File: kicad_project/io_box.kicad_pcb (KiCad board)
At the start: 4 copper layers, 200 x 120 mm, 76 parts, among them J1 24V, J10 24V, J2 GND, J3 Conn_01x02, J4 Output, J5 Digital Input, J6 5V, J7 12V, J8 NC, J9 GND, Q1 2N3904, Q2 2N3904, Q3 2N3904, Q4 2N3904, SW1 SW_Push, SW10 SW_Push, SW2 SW_Push, SW3 SW_Push, SW4 SW_SPDT, SW5 SW_SPDT, SW6 SW_DIP_x04, SW7 SW_SPDT, SW8 SW_DIP_x04, SW9 SW_SPDT, U1 R-78E5.0-1.0, U2 SN74AC14N, U3 R-78E12-1.0/X9

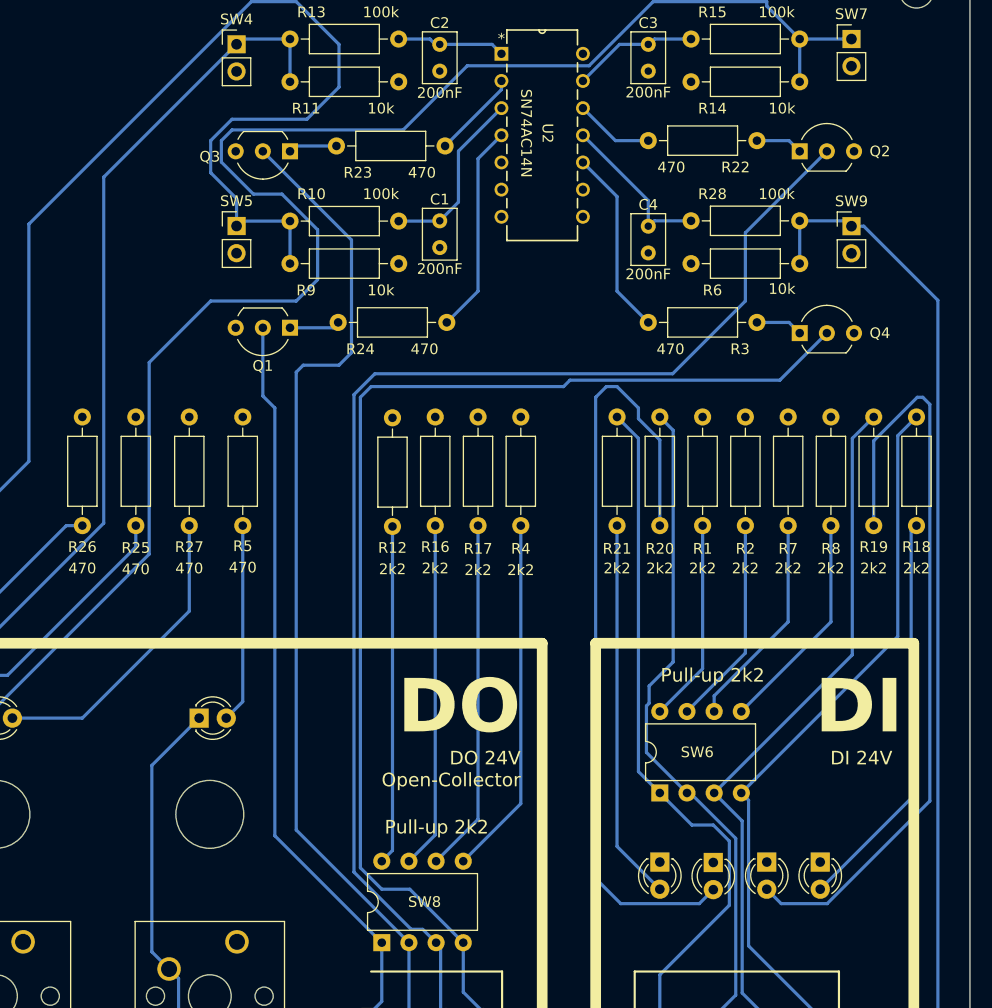
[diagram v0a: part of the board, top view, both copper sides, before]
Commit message: Bug fixes and resistor changes
Raised LED resistor values from 470 to 2k2 and from 2k2 to 10k.
Fixed NPN transistor incorrect pin order.
Fixed LPTA connector footprint pins.
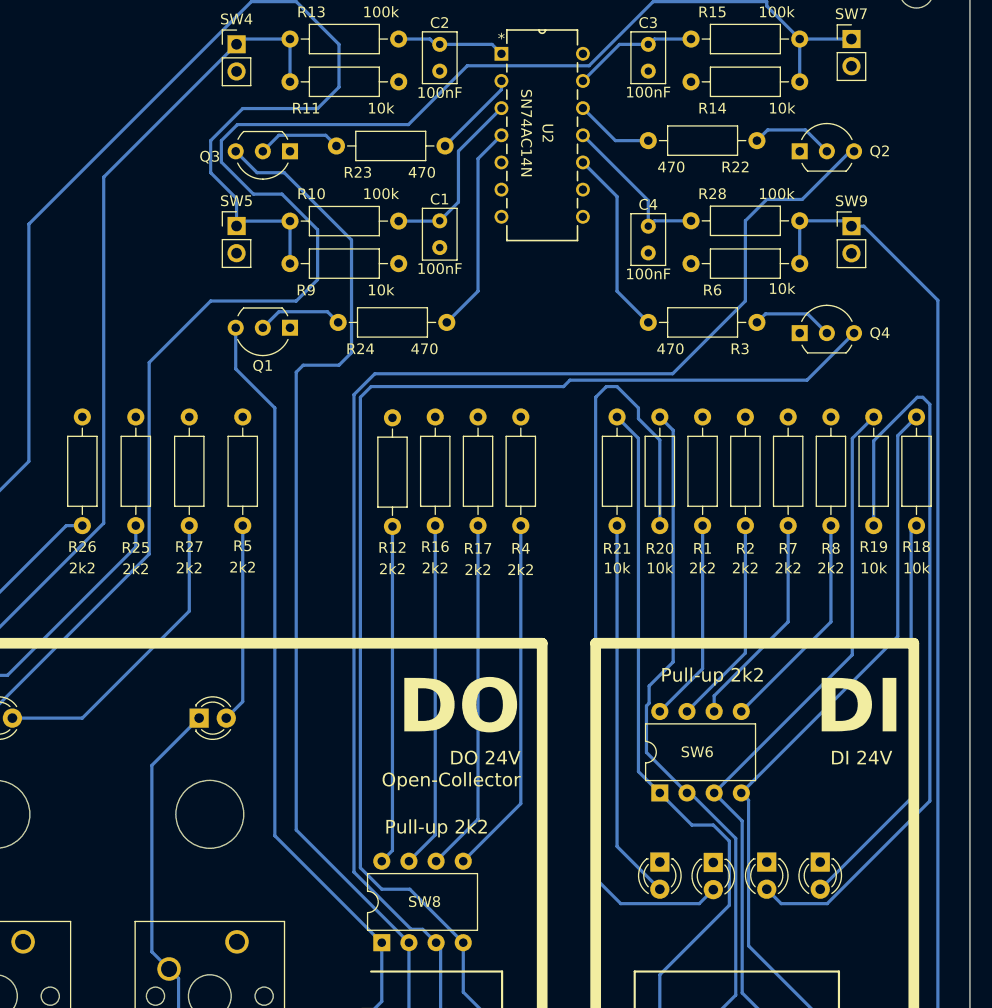
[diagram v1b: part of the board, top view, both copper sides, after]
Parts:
- C1, C2, C3, C4: value 200nF -> 100nF
- J10: value 24V -> 24V_BIG
- J3: value Conn_01x02 -> Power In
- J9: value GND -> GND_BIG
- R18, R19, R20, R21: value 2k2 -> 10k
- R25, R26, R27, R5: value 470 -> 2k2
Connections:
- Q1 pad 1: Net-(Q1-B) -> GND
- Q1 pad 2: /OUT_1_24V -> Net-(Q1-C)
- Q1 pad 3: GND -> /OUT_1_24V
- Q2 pad 1: Net-(Q2-B) -> GND
- Q2 pad 2: /OUT_3_24V -> Net-(Q2-C)
- Q2 pad 3: GND -> /OUT_3_24V
- Q3 pad 1: Net-(Q3-B) -> GND
- Q3 pad 2: /OUT_2_24V -> Net-(Q3-C)
- Q3 pad 3: GND -> /OUT_2_24V
- Q4 pad 1: Net-(Q4-B) -> GND
- Q4 pad 2: /OUT_4_24V -> Net-(Q4-C)
- Q4 pad 3: GND -> /OUT_4_24V
- R22 pad 2: Net-(Q2-B) -> Net-(Q2-C)
- R23 pad 2: Net-(Q3-B) -> Net-(Q3-C)
- R24 pad 2: Net-(Q1-B) -> Net-(Q1-C)
- R3 pad 2: Net-(Q4-B) -> Net-(Q4-C)
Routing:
- net Net-(Q1-C): track 0.00 -> 8.08 mm
- net Net-(Q3-C): track 0.00 -> 7.92 mm
- net Net-(Q2-C): track 0.00 -> 7.78 mm
- net Net-(Q4-C): track 0.00 -> 7.02 mm
- net Net-(Q1-B): track 4.71 -> 0.00 mm
- net Net-(Q3-B): track 4.55 -> 0.00 mm
- net Net-(Q4-B): track 4.41 -> 0.00 mm
- net Net-(Q2-B): track 4.41 -> 0.00 mm
- net /OUT_3_24V: track 119.8 -> 123.0 mm
- net /OUT_2_24V: track 92.9 -> 95.5 mm
- net /OUT_4_24V: track 110.4 -> 112.9 mm
- net /OUT_1_24V: track 69.5 -> 70.6 mm
